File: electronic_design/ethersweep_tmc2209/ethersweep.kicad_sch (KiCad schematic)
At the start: 98 parts, among them J1 AVR-ISP-6, J10 HR911105A, J2 Conn_01x02_Male, J3 Conn_01x04_Female, J4 Conn_01x02_Male, J5 Conn_01x02_Male, J6 Conn_01x07_Female, J7 Conn_01x07_Male, J8 AVR-ISP-6, J9 USB_B_Micro, SW1 SW_Push, U1 CP2102N-A01-GQFN28, U2 ATmega328-AU, U4 DD4012SA, U5 AS5600, U6 W5500, Y2 Crystal_25MHz, Y3 Crystal

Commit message: major commit for ethersweep 4 with STM32 MCU and USB C + fixes
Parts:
- removed C? (x3): C100nF, Capacitor_SMD:C_0805_2012Metric, symbol Device:C
- removed J4, J5: Conn_01x02_Male, Connector_JST:JST_EH_S2B-EH_1x02_P2.50mm_Horizontal, symbol Connector:Conn_01x02_Male
- removed R14, R15: R1k, Resistor_SMD:R_0603_1608Metric, symbol Device:R
- removed R24: R330, Resistor_SMD:R_0603_1608Metric, symbol Device:R
- removed U?: STM32F103RBTx, Package_QFP:LQFP-64_10x10mm_P0.5mm, symbol MCU_ST_STM32F1:STM32F103RBTx
- added C18, C22, C23, C28, C? (x4): C100nF, Capacitor_SMD:C_0402_1005Metric, symbol Device:C
- added C31: C10uF, Capacitor_SMD:C_0402_1005Metric, symbol Device:C
- added J12: USB_C_Receptacle, Connector_USB:USB_C_Receptacle_XKB_U262-16XN-4BVC11, symbol Connector:USB_C_Receptacle
- added J4, J5: Conn_01x03_Male, Connector_JST:JST_EH_S3B-EH_1x03_P2.50mm_Horizontal, symbol Connector:Conn_01x03_Male
- added R?: R1k, Resistor_SMD:R_0402_1005Metric, symbol Device:R
- added R?: R1M, Resistor_SMD:R_0402_1005Metric, symbol Device:R
- added R? (x4): R10k, Resistor_SMD:R_0402_1005Metric, symbol Device:R
- added TP5: BOOT_1, TestPoint:TestPoint_Pad_D2.0mm, symbol Connector:TestPoint
- added TP6: BOOT_0, TestPoint:TestPoint_Pad_D2.0mm, symbol Connector:TestPoint
- added U3: STM32F103C8Tx, Package_QFP:LQFP-48_7x7mm_P0.5mm, symbol MCU_ST_STM32F1:STM32F103C8Tx
- added U8: STUSB4500QTR, Package_CSP:ST_WLCSP-25_Die444, symbol Interface_USB:STUSB4500QTR
- C1, C12, C19, C20, C21, C27, C6: footprint Capacitor_SMD:C_0805_2012Metric -> Capacitor_SMD:C_0402_1005Metric; LCSC C49678 -> C307331
- C11: renamed from C?; footprint Capacitor_SMD:C_0805_2012Metric -> Capacitor_SMD:C_1206_3216Metric; LCSC C5378 -> C29823
- C13, C7: footprint Capacitor_SMD:C_0603_1608Metric -> Capacitor_SMD:C_0402_1005Metric
- C14, C15, C16, C17, C24, C25: LCSC C1525 -> C307331
- C29: footprint Capacitor_SMD:C_0805_2012Metric -> Capacitor_SMD:C_0402_1005Metric; LCSC C1525 -> C307331
- C30: footprint Capacitor_SMD:C_0805_2012Metric -> Capacitor_SMD:C_0603_1608Metric
- C35: footprint Capacitor_SMD:C_0603_1608Metric -> Capacitor_SMD:C_0402_1005Metric; LCSC C57112 -> C15195
- C9: renamed from C?; footprint Capacitor_SMD:C_0805_2012Metric -> Capacitor_SMD:C_0402; LCSC C1729 -> C1532
- R1, R16, R17, R2, R3: footprint Resistor_SMD:R_0603_1608Metric -> Resistor_SMD:R_0402_1005Metric
- R21: footprint Resistor_SMD:R_0603_1608Metric -> Resistor_SMD:R_0402_1005Metric; LCSC C17514 -> C26083
- R22: footprint Resistor_SMD:R_0603_1608Metric -> Resistor_SMD:R_0402_1005Metric; LCSC C30908 -> C316976
- R4, R5, R6, R7: footprint Resistor_SMD:R_0805_2012Metric -> Resistor_SMD:R_0603_1608Metric; LCSC C17634 -> C23140
- R8: footprint Resistor_SMD:R_0805_2012Metric -> Resistor_SMD:R_0603_1608Metric; LCSC C17415 -> C22859
- TP1: value TestPoint -> 3.3V
- TP2: value TestPoint -> GND
- TP3: value TestPoint -> RX
- TP4: value TestPoint -> TX
- U7: renamed from U?; footprint QFN28_5X5_TRI -> KiCad:TMC2209-LA
- gave numbers to parts that had none: 4
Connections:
- net +3.3VA: now also C20.1, C21.1, C18.1; no longer C14.1, C24.1, C25.1
- net +3V3: now also C14.1, C?.1, C?.1, C?.1, C?.1, J4.2 (Pin_2), J5.2 (Pin_2), R?.1, R?.1, R?.1, R?.1, U3.24 (VDD), U3.36 (VDD), U3.48 (VDD), U3.9 (VDDA); no longer C29.1
- net ENDSTOP: now also R1.2, J4.3 (Pin_3); no longer R2.2
- net ESTOP: now also R2.2, J5.3 (Pin_3); no longer R1.2
- net GND: now also C24.1, C27.2, C18.2, C22.1, C31.2, C?.2, C?.2, C?.2, C?.2, J12.A1 (GND), J12.A12 (GND), J12.B1 (GND), J12.B12 (GND), J4.1 (Pin_1), J5.1 (Pin_1), U3.23 (VSS), U3.35 (VSS), U3.47 (VSS), U3.8 (VSSA), U8.10 (GND), U8.25 (GND); no longer C24.2
- net SCL: now also R?.2
- net SDA: now also R?.2
- net rst: now also C22.2, C28.1, U3.7 (NRST); no longer C27.1
- net at C10.2, Y3.1: now also R?.1, U3.5 (PD0-OSC_IN); no longer U2.8 (XTAL2/PB7)
- net at C8.1, Y3.2: now also R?.2, U3.6 (PD0-OSC_OUT); no longer U2.7 (XTAL1/PB6)
- net at D2.2 (A): now also R?.1
- net at U1.28 (~{DTR}): now also C28.2; no longer C27.2
- net at U1.6 (VDD): now also C24.2; no longer C20.1
- net at J9.1 (VBUS), U1.7 (REGIN), U1.8 (VBUS): now also C25.1; no longer C21.1
- net at U7.6 (VCP): now also C23.2
- net +12V renamed +28V
- net +28V: now also C27.1, C29.1, C23.1, C31.1
- net DIR: no longer names the net of U2.10 (PD6)
- net FLT_STEPPER: no longer names the net of U2.26 (PC3)
- net M0: no longer names the net of U2.24 (PC1)
- net M1: no longer names the net of U2.23 (PC0)
- net M2: no longer names the net of U2.25 (PC2)
- net STEP: no longer names the net of U2.11 (PD7)
- net STEPPER_ENABLE: no longer names the net of U2.9 (PD5)
- new net: R?.2, U3.2 (PC13-TAMPER-RTC)
- new net: J12.A4 (VBUS), J12.A9 (VBUS), J12.B4 (VBUS), J12.B9 (VBUS)
- new net BOOT_0: R?.2, TP6.1, U3.44 (BOOT0)
- new net BOOT_1: R?.2, TP5.1, U3.20 (PB2)
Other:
- note added: "CP2102 USB / Serial conterver"
- note added: "Debug connectors"
- note added: "ENCODER"
- note added: "End and Emergency Stop"
- note added: "M3 mounts"
- note added: "PCB Bridge Connectorboard"
- note added: "PCB Bridge Mainboard"
- note added: "Power input and regulation"
- note added: "Pull UPs"
- note added: "Reset Button"
- note added: "TMC2209 Motor Controller"
- note added: "W5500 Ethernet Controller"
- note added: "up to 36.3V without destroying STM32F103c8 0,0886V resolution with 12Bit ADC when REF 3.3V"
- note removed: "PCB Bridge"
- note removed: "up to 36.3V without destroying a328p 0,035V resolution with 10Bit ADC"
- title: ETHERSWEEP 3 -> ETHERSWEEP 4
- moved on the sheet: C10, C11, C12, C13, C19, C2, C26, C3, C30, C33, C34, C35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

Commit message: cleanup, schmeatic design around USB connecotr, STM32 and reorganisation
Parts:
- removed C14, C19, C24, C25, C28: C100nF, Capacitor_SMD:C_0402_1005Metric, symbol Device:C
- removed J12: USB_C_Receptacle, Connector_USB:USB_C_Receptacle_XKB_U262-16XN-4BVC11, symbol Connector:USB_C_Receptacle
- removed J6: Conn_01x07_Female, Connector_PinHeader_2.54mm:PinHeader_1x07_P2.54mm_Vertical, symbol Connector:Conn_01x07_Female
- removed J7: Conn_01x07_Male, Connector_PinHeader_2.54mm:PinHeader_1x07_P2.54mm_Vertical, symbol Connector:Conn_01x07_Male
- removed J9: USB_B_Micro, Connector_USB:USB_Micro-B_Molex_47346-0001, symbol Connector:USB_B_Micro
- removed U1: CP2102N-A01-GQFN28, Package_DFN_QFN:QFN-28-1EP_5x5mm_P0.5mm_EP3.35x3.35mm, symbol Interface_USB:CP2102N-A01-GQFN28
- removed U2: ATmega328-AU, Package_QFP:TQFP-32_7x7mm_P0.8mm, symbol MCU_Microchip_ATmega:ATmega328-AU
- removed U8: STUSB4500QTR, Package_CSP:ST_WLCSP-25_Die444, symbol Interface_USB:STUSB4500QTR
- added C38: C100nF, Capacitor_SMD:C_0603_1608Metric, symbol Device:C
- added C39: C_330uF, Capacitor_SMD:CP_Elec_10x10, symbol Device:C_Polarized
- added C40: C10uF, Capacitor_SMD:C_1206_3216Metric, symbol Device:C
- added D5: D_TVS_5V, Diode_SMD:D_SMA, symbol Device:D_Schottky
- added D6: D_TVS_30V, Diode_SMD:D_SOD-123, symbol Device:D_Schottky
- added J12: USB_C_Receptacle_USB2.0, Connector_USB:USB_C_Receptacle_HRO_TYPE-C-31-M-12, symbol Connector:USB_C_Receptacle_USB2.0
- added J6: Conn_01x06_Female, Connector_PinHeader_2.54mm:PinHeader_1x06_P2.54mm_Vertical, symbol Connector:Conn_01x06_Female
- added J7: Conn_01x06_Male, Connector_PinHeader_2.54mm:PinHeader_1x06_P2.54mm_Vertical, symbol Connector:Conn_01x06_Male
- added R30: R1k, Resistor_SMD:R_0402_1005Metric, symbol Device:R
- added R31, R32: R22, Resistor_SMD:R_0402_1005Metric, symbol Device:R
- added R33, R34: R5.1k, Resistor_SMD:R_0402_1005Metric, symbol Device:R
- added R35: R1.5k, Resistor_SMD:R_0402_1005Metric, symbol Device:R
- C23, C27, C29, C6: footprint Capacitor_SMD:C_0402_1005Metric -> Capacitor_SMD:C_0603_1608Metric
- C30: footprint Capacitor_SMD:C_0603_1608Metric -> Capacitor_SMD:C_0805_2012Metric
- C31: footprint Capacitor_SMD:C_0402_1005Metric -> Capacitor_SMD:C_1206_3216Metric
- C36: LCSC C23733 -> C23733
- C9: footprint Capacitor_SMD:C_0402 -> Capacitor_SMD:C_0603_1608Metric; LCSC C1532 -> C21122
- R11, R12: value R180mOHM -> R100mOHM; footprint Resistor_SMD:R_1206_3216Metric -> Resistor_SMD:R_2010_5025Metric; LCSC C159408 -> C175979
- gave numbers to parts that had none: 10
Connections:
- net MOT_CLK is gone; now on net GND: U7.13 (CLK)
- net +28V: now also C39.1, C40.1, D6.1 (K)
- net +3V3: now also C38.1, R35.2; no longer R28.1, R29.1
- net ENDSTOP: now also J6.2 (Pin_2), J7.2 (Pin_2)
- net ESTOP: now also J6.1 (Pin_1), J7.1 (Pin_1)
- net ETH_INT: now also J6.6 (Pin_6), J7.6 (Pin_6)
- net GND: now also R28.1, R29.1, C38.2, C39.2, C40.2, D5.2 (A), D6.2 (A), J12.A1 (GND), J12.A12 (GND), J12.B1 (GND), J12.B12 (GND), J12.S1 (SHIELD), R33.2, R34.2
- net MISO: now also U3.16 (PA6)
- net MOSI: now also U3.17 (PA7)
- net RST_ETHERNET: now also J6.5 (Pin_5), J7.5 (Pin_5)
- net SCK: now also U3.15 (PA5)
- net SCL: now also U3.42 (PB6), J6.3 (Pin_3), J7.3 (Pin_3)
- net SDA: now also U3.43 (PB7), J6.4 (Pin_4), J7.4 (Pin_4)
- net uC_RX: now also U3.31 (PA10)
- net uC_TX: now also U3.30 (PA9)
- net voltage_detect: now also U3.11 (PA1)
- net MOT_VREF_POT: now reaches RV1.2, U7.17 (VREF)
- net MOT_VREF_POT: now also U3.12 (PA2)
- net at C11.1, U7.8 (5VOUT): now also D5.1 (K)
- net USB-: now reaches U3.32 (PA11)
- net USB-: now also R31.2
- net USB+: now reaches U3.33 (PA12)
- net USB+: now also R32.2
- net MOT_UART_PDN renamed MOT_UART_RX
- net MOT_UART_RX: now also R30.2
- new net: J12.A5 (CC1), R33.1
- new net: J12.A6 (D+), J12.B6 (D+), R32.1, R35.1
- new net: J12.A7 (D-), J12.B7 (D-), R31.1
- new net: J12.B5 (CC2), R34.1
- new net: J12.A4 (VBUS), J12.A9 (VBUS), J12.B4 (VBUS), J12.B9 (VBUS)
- new net MOT_UART_TX: R30.1
- no-connect marks 0 -> 2
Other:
- note added: "Pull UPs Downs"
- note added: "USB"
- note removed: "CP2102 USB / Serial conterver"
- note removed: "Pull UPs"
- moved on the sheet: C1, C11, C12, C13, C15, C16, C17, C18, C2, C20, C21, C22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

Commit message: layout version 4 in manufacturable state: STM32, TMC2209, USBC, 3 pin switches
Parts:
- removed C29: C100nF, Capacitor_SMD:C_0603_1608Metric, symbol Device:C
- removed J11: Conn_01x04_Male, Connector_JST:JST_EH_S4B-EH_1x04_P2.50mm_Horizontal, symbol Connector:Conn_01x04_Male
- removed RV1: R_POT_20K, Potentiometer_SMD:Potentiometer_Bourns_TC33X_Vertical, symbol Device:R_POT
- added J9: Conn_01x04_Female, Connector_JST:JST_EH_S4B-EH_1x04_P2.50mm_Horizontal, symbol Connector:Conn_01x04_Female
- C9: footprint Capacitor_SMD:C_0603_1608Metric -> Capacitor_SMD:C_0402_1005Metric; LCSC C21122 -> C1532
- D5: footprint Diode_SMD:D_SMA -> Diode_SMD:D_SOD-123; LCSC C2925443 -> C478011
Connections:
- net ENDSTOP: now also U3.13 (PA3)
- net ESTOP: now also U3.14 (PA4)
- net ETH_INT: now also U3.18 (PB0)
- net MOT_DIR: now also U3.38 (PA15)
- net MOT_SPREAD: now also U3.46 (PB9)
- net MOT_STANDBY: now also U3.37 (PA14)
- net MOT_STEP: now also U3.45 (PB8)
- net MOT_UART_RX: now also U3.21 (PB10)
- net MOT_UART_TX: now also U3.22 (PB11)
- net RST_ETHERNET: now also U3.19 (PB1)
- net at U7.21 (OA2): now also J9.4 (Pin_4)
- net at U7.26 (OB1): now also J9.2 (Pin_2)
- net at U7.24 (OA1): now also J9.3 (Pin_3)
- net at U7.1 (OB2): now also J9.1 (Pin_1)
- net MOT_VREF_POT: no longer names the net of U7.17 (VREF)
- net MOT_VREF_POT: no longer U3.12 (PA2)
- no-connect marks 2 -> 3
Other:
- moved on the sheet: C1, C10, C11, C12, C13, C14, C15, C16, C17, C18, C19, C2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

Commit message: minor design changes
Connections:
- net RST_ETHERNET: now also U3.11 (PA1); no longer U3.19 (PB1)
- net voltage_detect: now also U3.19 (PB1); no longer U3.11 (PA1)
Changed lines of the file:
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@@
-    (stroke (width 0) (type default) (color 0 0 0 0))
-  )
-  (wire (pts (xy 104.14 86.106) (xy 112.395 86.106))
     (stroke (width 0) (type default) (color 0 0 0 0))
   )
@@
     (stroke (width 0) (type default) (color 0 0 0 0))
   )
+  (wire (pts (xy 104.14 86.106) (xy 108.712 86.106))
+    (stroke (width 0) (type default) (color 0 0 0 0))
+  )
   (wire (pts (xy 178.308 51.562) (xy 180.848 51.562))
     (stroke (width 0) (type default) (color 0 0 0 0))
@@
     (stroke (width 0) (type default) (color 0 0 0 0))
   )
+  (wire (pts (xy 71.12 86.106) (xy 62.992 86.106))
+    (stroke (width 0) (type default) (color 0 0 0 0))
+  )
   (wire (pts (xy 464.82 88.9) (xy 458.47 88.9))
     (stroke (width 0) (type default) (color 0 0 0 0))
@@
   )
   (wire (pts (xy 230.378 126.492) (xy 230.378 129.032))
-    (stroke (width 0) (type default) (color 0 0 0 0))
-  )
-  (wire (pts (xy 71.12 86.106) (xy 66.548 86.106))
     (stroke (width 0) (type default) (color 0 0 0 0))
   )
@@
     )
   )
+  (global_label "RST_ETHERNET" (shape input) (at 108.712 86.106 0) (fields_autoplaced)
+    (effects (font (size 1.27 1.27)) (justify left))
+    (property "Intersheet References" "${INTERSHEET_REFS}" (id 0) (at 26.162 34.036 0)
+      (effects (font (size 1.27 1.27)) hide)
+    )
+  )
   (global_label "ENDSTOP" (shape input) (at 331.089 192.405 270) (fields_autoplaced)
     (effects (font (size 1.27 1.27)) (justify right))
@@
     )
   )
-  (global_label "voltage_detect" (shape input) (at 112.395 86.106 0) (fields_autoplaced)
-    (effects (font (size 1.27 1.27)) (justify left))
-    (property "Intersheet References" "${INTERSHEET_REFS}" (id 0) (at 146.685 140.716 0)
+  (global_label "voltage_detect" (shape input) (at 62.992 86.106 180) (fields_autoplaced)
+    (effects (font (size 1.27 1.27)) (justify right))
+    (property "Intersheet References" "${INTERSHEET_REFS}" (id 0) (at 28.702 31.496 0)
       (effects (font (size 1.27 1.27)) hide)
     )
@@
     )
   )
-  (global_label "RST_ETHERNET" (shape input) (at 66.548 86.106 180) (fields_autoplaced)
-    (effects (font (size 1.27 1.27)) (justify right))
-    (property "Intersheet References" "${INTERSHEET_REFS}" (id 0) (at 149.098 138.176 0)
-      (effects (font (size 1.27 1.27)) hide)
-    )
-  )

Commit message: pcb design changes, reorganisation, JLC part number assignments, size corrections
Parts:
- C1: footprint Capacitor_SMD:C_0402_1005Metric -> Capacitor_SMD:C_0603_1608Metric; LCSC C307331 -> C14663
- C23, C27, C38, C6: LCSC C307331 -> C14663
- D3, D4: LCSC C2286 -> C2296
- J12: LCSC (none) -> C165948
- R1, R15, R2: footprint Resistor_SMD:R_0402_1005Metric -> Resistor_SMD:R_0603_1608Metric
- R16, R24, R27, R28, R29, R3: LCSC C25804 -> C25744
- R17, R30: LCSC C21190 -> C11702
- U3: LCSC (none) -> C8734
- U7: LCSC (none) -> C465949
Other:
- note added: "STM32 Microcontroller"
- note added: "up to 36.3V without destroying STM32F103c8 0,0886V resolution with 12Bit ADC when aREF 3.3V"
- note removed: "up to 36.3V without destroying STM32F103c8 0,0886V resolution with 12Bit ADC when REF 3.3V"
- moved on the sheet: C10, C14, C19, C32, C37, C8, D2, H1, H2, H3, H4, H5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

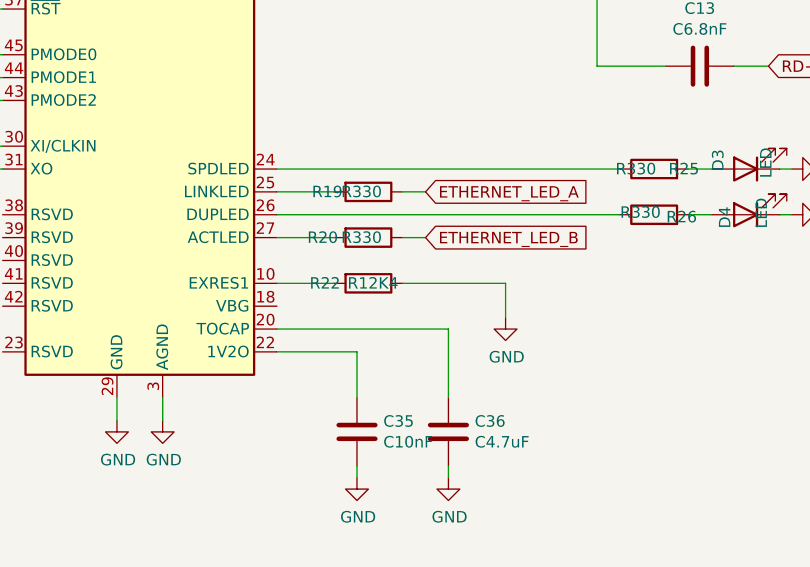
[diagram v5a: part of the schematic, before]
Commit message: part assignments, minor part changes
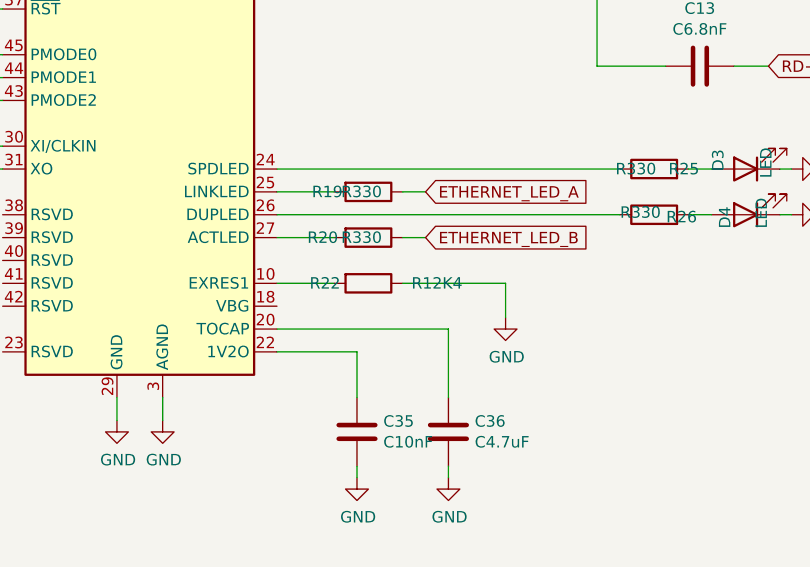
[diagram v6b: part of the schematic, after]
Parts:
- R22: footprint Resistor_SMD:R_0402_1005Metric -> Resistor_SMD:R_0603_1608Metric; LCSC C316976 -> C234268
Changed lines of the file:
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@@
     (in_bom yes) (on_board yes)
     (property "Reference" "R22" (id 0) (at 253.492 113.792 90))
-    (property "Value" "R12K4" (id 1) (at 258.826 113.792 90))
-    (property "Footprint" "Resistor_SMD:R_0402_1005Metric" (id 2) (at 258.318 112.014 90)
+    (property "Value" "R12K4" (id 1) (at 265.938 113.792 90))
+    (property "Footprint" "Resistor_SMD:R_0603_1608Metric" (id 2) (at 258.318 112.014 90)
       (effects (font (size 1.27 1.27)) hide)
     )
@@
       (effects (font (size 1.27 1.27)) hide)
     )
-    (property "LCSC" "C316976" (id 4) (at 258.318 113.792 90)
+    (property "LCSC" "C234268" (id 4) (at 258.318 113.792 90)
       (effects (font (size 1.27 1.27)) hide)
     )
@@
     )
     (path "/00000000-0000-0000-0000-0000613a10c7"
-      (reference "R22") (unit 1) (value "R12K4") (footprint "Resistor_SMD:R_0402_1005Metric")
+      (reference "R22") (unit 1) (value "R12K4") (footprint "Resistor_SMD:R_0603_1608Metric")
     )
     (path "/00000000-0000-0000-0000-0000619474df"
